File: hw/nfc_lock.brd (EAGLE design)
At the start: 100 x 80 mm, 8 parts, among them IC1 STM8S003F3, IC3 MCP170312MB, U1 M24SR16-YMN6T/2, X1 MINI-USB-32005-301

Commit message: added capacitors values
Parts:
- C2: value (none) -> 4.7uF
- C3: value (none) -> 100nF
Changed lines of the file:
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@@
 <layer number="48" name="Document" color="7" fill="1" visible="yes" active="yes"/>
 <layer number="49" name="Reference" color="7" fill="1" visible="yes" active="yes"/>
+<layer number="50" name="dxf" color="7" fill="1" visible="no" active="yes"/>
 <layer number="51" name="tDocu" color="7" fill="1" visible="yes" active="yes"/>
 <layer number="52" name="bDocu" color="7" fill="1" visible="yes" active="yes"/>
+<layer number="53" name="tGND_GNDA" color="7" fill="9" visible="no" active="no"/>
+<layer number="54" name="bGND_GNDA" color="1" fill="9" visible="no" active="no"/>
+<layer number="56" name="wert" color="7" fill="1" visible="no" active="yes"/>
+<layer number="57" name="tCAD" color="7" fill="1" visible="no" active="no"/>
+<layer number="59" name="tCarbon" color="7" fill="1" visible="no" active="no"/>
+<layer number="60" name="bCarbon" color="7" fill="1" visible="no" active="no"/>
 <layer number="90" name="Modules" color="5" fill="1" visible="no" active="no"/>
 <layer number="91" name="Nets" color="2" fill="1" visible="no" active="no"/>
@@
 <layer number="98" name="Guide" color="6" fill="1" visible="no" active="no"/>
 <layer number="99" name="SpiceOrder" color="5" fill="1" visible="no" active="no"/>
+<layer number="100" name="Muster" color="7" fill="1" visible="no" active="no"/>
+<layer number="101" name="Patch_Top" color="12" fill="4" visible="no" active="yes"/>
+<layer number="102" name="Vscore" color="7" fill="1" visible="no" active="yes"/>
+<layer number="103" name="fp3" color="7" fill="1" visible="no" active="yes"/>
+<layer number="104" name="Name" color="7" fill="1" visible="no" active="yes"/>
+<layer number="105" name="Beschreib" color="9" fill="1" visible="no" active="yes"/>
+<layer number="106" name="BGA-Top" color="4" fill="1" visible="no" active="yes"/>
+<layer number="107" name="BD-Top" color="5" fill="1" visible="no" active="yes"/>
+<layer number="108" name="fp8" color="7" fill="1" visible="no" active="yes"/>
+<layer number="109" name="fp9" color="7" fill="1" visible="no" active="yes"/>
+<layer number="110" name="fp0" color="7" fill="1" visible="no" active="yes"/>
+<layer number="111" name="LPC17xx" color="7" fill="1" visible="no" active="yes"/>
+<layer number="112" name="tSilk" color="7" fill="1" visible="no" active="yes"/>
+<layer number="113" name="ReferenceLS" color="7" fill="1" visible="no" active="no"/>
+<layer number="116" name="Patch_BOT" color="9" fill="4" visible="no" active="yes"/>
+<layer number="118" name="Rect_Pads" color="7" fill="1" visible="no" active="no"/>
+<layer number="121" name="_tsilk" color="7" fill="1" visible="no" active="yes"/>
+<layer number="122" name="_bsilk" color="7" fill="1" visible="no" active="yes"/>
+<layer number="123" name="tTestmark" color="7" fill="1" visible="no" active="yes"/>
+<layer number="124" name="bTestmark" color="7" fill="1" visible="no" active="yes"/>
+<layer number="125" name="_tNames" color="7" fill="1" visible="no" active="yes"/>
+<layer number="126" name="_bNames" color="7" fill="1" visible="no" active="yes"/>
+<layer number="127" name="_tValues" color="7" fill="1" visible="no" active="yes"/>
+<layer number="128" name="_bValues" color="7" fill="1" visible="no" active="yes"/>
+<layer number="129" name="Mask" color="7" fill="1" visible="yes" active="yes"/>
+<layer number="131" name="tAdjust" color="7" fill="1" visible="no" active="yes"/>
+<layer number="132" name="bAdjust" color="7" fill="1" visible="no" active="yes"/>
+<layer number="144" name="Drill_legend" color="7" fill="1" visible="no" active="yes"/>
+<layer number="150" name="Notes" color="7" fill="1" visible="no" active="yes"/>
+<layer number="151" name="HeatSink" color="7" fill="1" visible="no" active="yes"/>
+<layer number="152" name="_bDocu" color="7" fill="1" visible="no" active="yes"/>
+<layer number="153" name="FabDoc1" color="6" fill="1" visible="no" active="no"/>
+<layer number="154" name="FabDoc2" color="2" fill="1" visible="no" active="no"/>
+<layer number="155" name="FabDoc3" color="7" fill="15" visible="no" active="no"/>
+<layer number="199" name="Contour" color="7" fill="1" visible="no" active="yes"/>
+<layer number="200" name="200bmp" color="1" fill="10" visible="no" active="yes"/>
+<layer number="201" name="201bmp" color="2" fill="1" visible="no" active="no"/>
+<layer number="202" name="202bmp" color="3" fill="1" visible="no" active="no"/>
+<layer number="203" name="203bmp" color="4" fill="10" visible="no" active="yes"/>
+<layer number="204" name="204bmp" color="5" fill="10" visible="no" active="yes"/>
+<layer number="205" name="205bmp" color="6" fill="10" visible="no" active="yes"/>
+<layer number="206" name="206bmp" color="7" fill="10" visible="no" active="yes"/>
+<layer number="207" name="207bmp" color="8" fill="10" visible="no" active="yes"/>
+<layer number="208" name="208bmp" color="9" fill="10" visible="no" active="yes"/>
+<layer number="209" name="209bmp" color="7" fill="1" visible="no" active="yes"/>
+<layer number="210" name="210bmp" color="7" fill="1" visible="no" active="yes"/>
+<layer number="211" name="211bmp" color="7" fill="1" visible="no" active="yes"/>
+<layer number="212" name="212bmp" color="7" fill="1" visible="no" active="yes"/>
+<layer number="213" name="213bmp" color="7" fill="1" visible="no" active="yes"/>
+<layer number="214" name="214bmp" color="7" fill="1" visible="no" active="yes"/>
+<layer number="215" name="215bmp" color="7" fill="1" visible="no" active="yes"/>
+<layer number="216" name="216bmp" color="7" fill="1" visible="no" active="yes"/>
+<layer number="217" name="217bmp" color="18" fill="1" visible="no" active="no"/>
+<layer number="218" name="218bmp" color="19" fill="1" visible="no" active="no"/>
+<layer number="219" name="219bmp" color="20" fill="1" visible="no" active="no"/>
+<layer number="220" name="220bmp" color="21" fill="1" visible="no" active="no"/>
+<layer number="221" name="221bmp" color="22" fill="1" visible="no" active="no"/>
+<layer number="222" name="222bmp" color="23" fill="1" visible="no" active="no"/>
+<layer number="223" name="223bmp" color="24" fill="1" visible="no" active="no"/>
+<layer number="224" name="224bmp" color="25" fill="1" visible="no" active="no"/>
+<layer number="225" name="225bmp" color="7" fill="1" visible="yes" active="yes"/>
+<layer number="226" name="226bmp" color="7" fill="1" visible="yes" active="yes"/>
+<layer number="227" name="227bmp" color="7" fill="1" visible="yes" active="yes"/>
+<layer number="228" name="228bmp" color="7" fill="1" visible="yes" active="yes"/>
+<layer number="229" name="229bmp" color="7" fill="1" visible="yes" active="yes"/>
+<layer number="230" name="230bmp" color="7" fill="1" visible="yes" active="yes"/>
+<layer number="231" name="Eagle3D_PG1" color="7" fill="1" visible="no" active="no"/>
+<layer number="232" name="Eagle3D_PG2" color="7" fill="1" visible="no" active="no"/>
+<layer number="233" name="Eagle3D_PG3" color="7" fill="1" visible="no" active="no"/>
+<layer number="248" name="Housing" color="7" fill="1" visible="no" active="yes"/>
+<layer number="249" name="Edge" color="7" fill="1" visible="no" active="yes"/>
+<layer number="250" name="Descript" color="7" fill="1" visible="no" active="no"/>
+<layer number="251" name="SMDround" color="7" fill="1" visible="no" active="no"/>
+<layer number="254" name="cooling" color="7" fill="1" visible="no" active="yes"/>
+<layer number="255" name="routoute" color="7" fill="1" visible="yes" active="yes"/>
 </layers>
 <board>
@@
 <element name="IC1" library="stm8" package="TSSOP20" value="STM8S003F3" x="31.75" y="35.56" rot="R270"/>
 <element name="IC3" library="linear" package="SOT89" value="MCP170312MB" x="43.18" y="48.26"/>
-<element name="C2" library="rcl" package="153CLV-0405" value="" x="36.83" y="48.26" rot="R90"/>
-<element name="C3" library="rcl" package="C1206" value="" x="43.18" y="41.91" rot="R180"/>
+<element name="C2" library="rcl" package="153CLV-0405" value="4.7uF" x="36.83" y="48.26" rot="R90"/>
+<element name="C3" library="rcl" package="C1206" value="100nF" x="43.18" y="41.91" rot="R180"/>
 <element name="D1" library="diode" package="SMA-DO214AC" value="GF1" x="31.75" y="52.07" rot="R90"/>
 <element name="D2" library="diode" package="SMA-DO214AC" value="GF1" x="41.91" y="54.61"/>

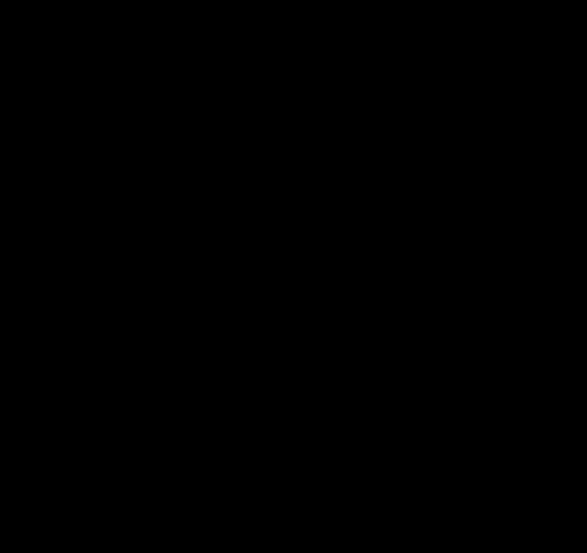
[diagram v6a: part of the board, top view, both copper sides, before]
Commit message: added more lines and power n-mosfet to schema
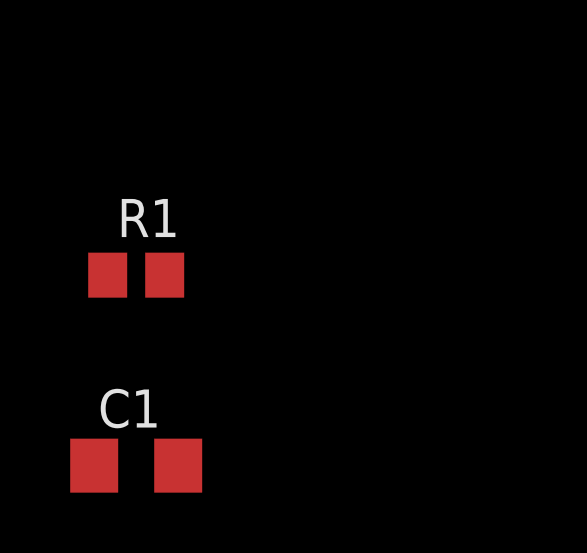
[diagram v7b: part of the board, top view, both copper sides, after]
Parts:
- added C1: 10nF, rcl:C1206
- added R1: 10k, rcl:R0805
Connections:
- new net N$5: C1.1, IC1.4, R1.2
- new net N$6: IC1.18
- new net N$7: IC1.10, U1.1
- new net N$8: IC1.13, U1.7
- net +5V/1: now also R1.1
- net 0V: now also C1.2
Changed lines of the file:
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@@
 <attribute name="OC_NEWARK" value="unknown" x="22.86" y="50.8" size="1.778" layer="27" display="off"/>
 </element>
+<element name="R1" library="rcl" package="R0805" value="10k" x="2.54" y="-21.59"/>
+<element name="C1" library="rcl" package="C1206" value="10nF" x="2.54" y="-27.94"/>
 </elements>
 <signals>
@@
 <contactref element="IC1" pad="7"/>
 <contactref element="U1" pad="4"/>
+<contactref element="C1" pad="2"/>
 <wire x1="41.78" y1="41.91" x2="41.681" y2="46.279" width="0" layer="19" extent="1-1"/>
 <wire x1="36.83" y1="46.46" x2="41.681" y2="46.279" width="0" layer="19" extent="1-1"/>
@@
 <wire x1="28.8322" y1="34.585" x2="36.83" y2="46.46" width="0" layer="19" extent="1-1"/>
 <wire x1="29.3878" y1="24.765" x2="28.8322" y2="34.585" width="0" layer="19" extent="1-1"/>
+<wire x1="3.94" y1="-27.94" x2="29.3878" y2="24.765" width="0" layer="19" extent="1-1"/>
 </signal>
 <signal name="+5V/1">
@@
 <contactref element="IC1" pad="9"/>
 <contactref element="U1" pad="8"/>
+<contactref element="R1" pad="1"/>
 <wire x1="44.58" y1="41.91" x2="44.679" y2="46.279" width="0" layer="19" extent="1-1"/>
-<wire x1="28.8322" y1="33.285" x2="44.58" y2="41.91" width="0" layer="19" extent="1-1"/>
-<wire x1="34.1122" y1="28.575" x2="28.8322" y2="33.285" width="0" layer="19" extent="1-1"/>
+<wire x1="34.1122" y1="28.575" x2="44.58" y2="41.91" width="0" layer="19" extent="1-1"/>
+<wire x1="28.8322" y1="33.285" x2="34.1122" y2="28.575" width="0" layer="19" extent="1-1"/>
+<wire x1="1.59" y1="-21.59" x2="34.1122" y2="28.575" width="0" layer="19" extent="1-1"/>
 </signal>
 <signal name="+5V">
@@
 <wire x1="43.96" y1="54.61" x2="43.18" y2="49.2" width="0" layer="19" extent="1-1"/>
 </signal>
+<signal name="N$5">
+<contactref element="C1" pad="1"/>
+<contactref element="R1" pad="2"/>
+<contactref element="IC1" pad="4"/>
+<wire x1="3.49" y1="-21.59" x2="28.8322" y2="36.535" width="0" layer="19" extent="1-1"/>
+<wire x1="1.14" y1="-27.94" x2="3.49" y2="-21.59" width="0" layer="19" extent="1-1"/>
+</signal>
+<signal name="N$6">
+<contactref element="IC1" pad="18"/>
+</signal>
+<signal name="N$7">
+<contactref element="IC1" pad="10"/>
+<contactref element="U1" pad="1"/>
+<wire x1="29.3878" y1="28.575" x2="28.8322" y2="32.635" width="0" layer="19" extent="1-1"/>
+</signal>
+<signal name="N$8">
+<contactref element="IC1" pad="13"/>
+<contactref element="U1" pad="7"/>
+<wire x1="34.1122" y1="27.305" x2="34.6678" y2="33.935" width="0" layer="19" extent="1-1"/>
+</signal>
 </signals>
